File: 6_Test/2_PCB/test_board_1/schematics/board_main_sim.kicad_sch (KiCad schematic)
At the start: 1 part

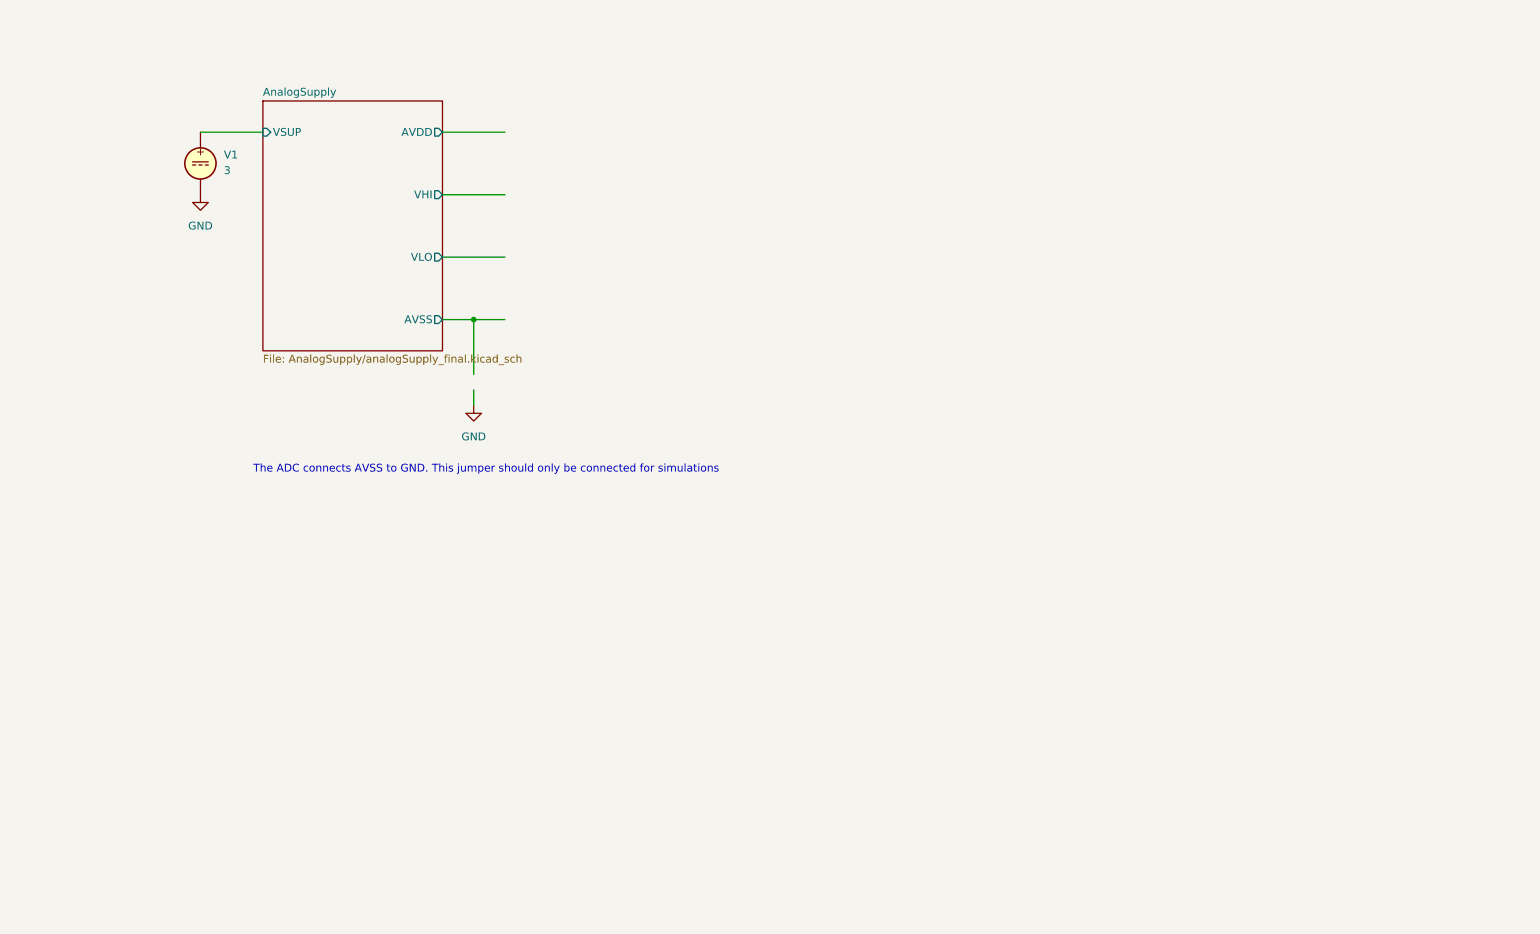
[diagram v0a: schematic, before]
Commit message: fixed digital supply, added three sheets to board main
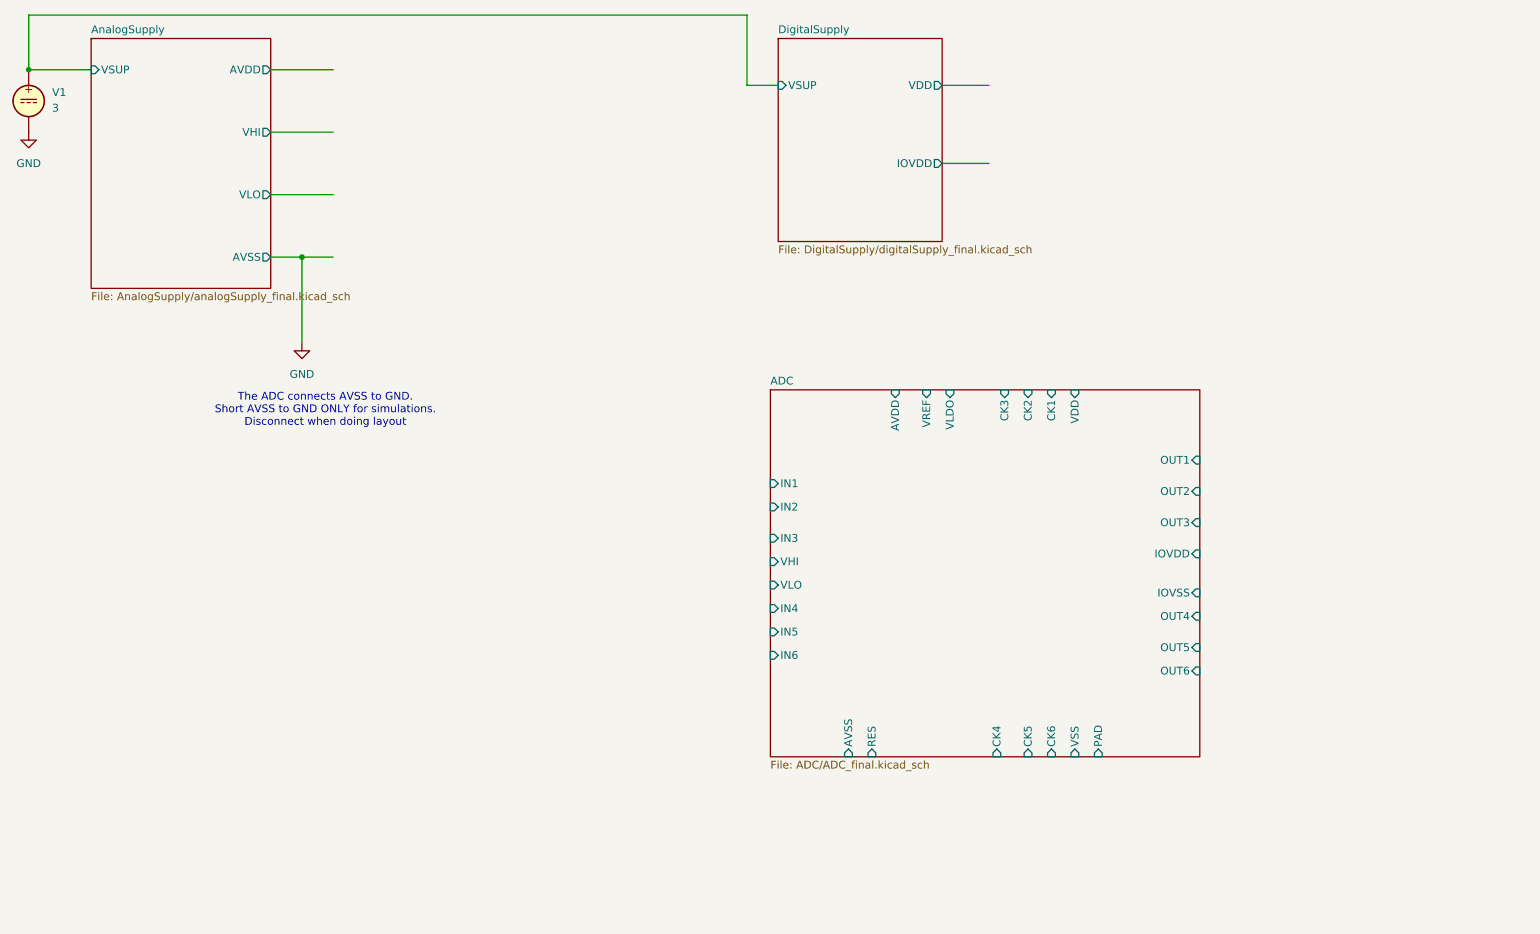
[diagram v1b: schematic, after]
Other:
- added sheet ADC (ADC/ADC_final.kicad_sch)
- added sheet DigitalSupply (DigitalSupply/digitalSupply_final.kicad_sch)
- note added: "The ADC connects AVSS to GND. Short AVSS to GND ONLY for simulations. Disconnect when doing layout"
- note removed: "The ADC connects AVSS to GND. This jumper should only be connected for simulations"
- moved on the sheet: V1

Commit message: final draft of board done.
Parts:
- added V2: 2, symbol Simulation_SPICE:VDC
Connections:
- net GND: now also V2.2
- new net Buffer/DI1: V2.1
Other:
- added sheet Buffer (Buffer/buffer_final.kicad_sch)
- added sheet ResetPulse (ResetPulse/reset_pulse_final.kicad_sch)
- note added: "Should model the digital output voltage from the ADC"
